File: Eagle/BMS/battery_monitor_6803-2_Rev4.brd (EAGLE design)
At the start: 69.5 x 53.3 mm, 66 parts, among them Q1 MOSFET-PCHANNELIRLML2244, Q10 IRF9530, Q2 MOSFET-NCHANNELBSS138, Q3 MOSFET-PCHANNELIRLML2244, Q4 MOSFET-PCHANNELIRLML2244, Q5 MOSFET-PCHANNELIRLML2244, Q6 MOSFET-NCHANNELBSS138, Q7 MOSFET-NCHANNELBSS138, Q8 MOSFET-NCHANNELBSS138, Q9 PMOS_AO4435

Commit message: Finished new BMS boards in Eagle.
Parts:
- moved R18 68.6 mm to (82.4, 51.4), turned to 90 degrees
- moved LED3 67.0 mm to (82.4, 48.6), turned to 180 degrees
- moved R17 65.7 mm to (80.1, 51.4), turned to 90 degrees
- moved LED2 64.0 mm to (80.1, 48.6), turned to 180 degrees
- moved R16 62.9 mm to (77.9, 51.4), turned to 90 degrees
- moved LED1 61.1 mm to (77.9, 48.6), turned to 180 degrees
- moved U$1 58.8 mm to (73.9, 34.8), turned to 0 degrees
- moved U$3 47.4 mm to (86.4, 34.8), turned to 0 degrees
- moved U$2 47.1 mm to (80.1, 34.8), turned to 180 degrees
- moved R24 1.73 mm to (30.7, 17.4)
- moved R23 1.53 mm to (33.0, 17.4)
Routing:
- net N$10: track 0.00 -> 83.7 mm, vias 0 -> 1
- net N$3: track 55.4 -> 133.8 mm, vias 2 -> 5
- net +5: track 71.0 -> 144.2 mm, vias 3 -> 4
- net N$12: track 0.00 -> 54.9 mm, vias 0 -> 2
- net GPIO2: track 0.00 -> 46.1 mm, vias 0 -> 3
- net N$2: track 36.2 -> 75.3 mm, vias 0 -> 2
- net N$5: track 0.00 -> 38.1 mm, vias 0 -> 1
- net GPIO1: track 0.00 -> 37.6 mm, vias 0 -> 4
- net A0: track 4.24 -> 41.8 mm, vias 1 -> 3
- net WDTB: track 0.00 -> 35.9 mm, vias 0 -> 4
- net N$29: track 0.00 -> 15.1 mm, vias 0 -> 2
- net S2: track 48.4 -> 36.9 mm, vias 3 -> 1
- net C12: track 41.9 -> 52.4 mm
- net SDA: track 57.0 -> 64.6 mm
- net VREF: track 29.7 -> 22.8 mm, vias 2 -> 3
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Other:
- board size 69.5 x 53.3 mm -> 89.8 x 53.3 mm
- board text added: "ITEST BMS Rev 4"
- board text removed: "ITEST BMS Rev 3"

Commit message: Final revisions on BMS boards.
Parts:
- moved U$1 0.28 mm to (74.0, 35.1)
- moved U$2 0.25 mm to (80.1, 35.1)
- moved U$3 0.25 mm to (86.4, 35.1)
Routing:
- net GND: track 137.4 -> 161.4 mm, vias 14 -> 13
- net N$3: track 133.8 -> 141.2 mm, vias 5 -> 6
- net N$12: track 54.9 -> 60.6 mm, vias 2 -> 1
- net CHARGER_IN: track 69.9 -> 64.9 mm
- net N$5: track 38.1 -> 35.6 mm
- net C1: track 87.5 -> 85.5 mm, vias 9 -> 6
- net ESTOP2: track 55.2 -> 53.5 mm, vias 4 -> 2
- net N$10: track 83.7 -> 82.4 mm
- net N$2: track 75.3 -> 74.4 mm, vias 2 -> 1
- net C2: track 87.7 -> 88.4 mm
- net S3: track 43.6 -> 43.1 mm
- net BATTERY+: track 16.2 -> 16.0 mm, vias 1 -> 0
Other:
- board size 89.8 x 53.3 mm -> 88.1 x 53.3 mm

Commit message: Latest BMS Rev3 and Rev4 edits.
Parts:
- R26: value 1MEG -> 1Meg
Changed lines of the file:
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@@
 <attribute name="PROD_ID" value="TRANS-11153" x="-74.168" y="-48.514" size="1.778" layer="27" rot="R270" display="off"/>
 <attribute name="NAME" x="47.625" y="41.9735" size="0.4064" layer="25" rot="R270"/>
-<attribute name="OC_NEWARK" value="40X8697" x="46.482" y="42.926" size="1.778" layer="27" rot="R270" display="off"/>
+<attribute name="OC_NEWARK" value="40T7448" x="46.482" y="42.926" size="1.778" layer="27" rot="R270" display="off"/>
 <attribute name="MF" value="" x="46.482" y="42.926" size="1.778" layer="27" rot="R270" display="off"/>
-<attribute name="MPN" value="SI2369DS-T1-GE3" x="46.482" y="42.926" size="1.778" layer="27" rot="R270" display="off"/>
+<attribute name="MPN" value="IRLML2244TRPBF" x="46.482" y="42.926" size="1.778" layer="27" rot="R270" display="off"/>
 </element>
 <element name="DZ1" library="SparkFun-DiscreteSemi" package="SOD-323" value="PDZ7.5B" x="34.798" y="46.482" smashed="yes" rot="R90">
@@
 <attribute name="PROD_ID" value="TRANS-11153" x="-87.63" y="21.209" size="1.778" layer="27" rot="R270" display="off"/>
 <attribute name="NAME" x="40.513" y="42.1005" size="0.4064" layer="25" rot="R270"/>
-<attribute name="OC_NEWARK" value="40X8697" x="39.37" y="42.799" size="1.778" layer="27" rot="R270" display="off"/>
+<attribute name="OC_NEWARK" value="40T7448" x="39.37" y="42.799" size="1.778" layer="27" rot="R270" display="off"/>
 <attribute name="MF" value="" x="39.37" y="42.799" size="1.778" layer="27" rot="R270" display="off"/>
-<attribute name="MPN" value="SI2369DS-T1-GE3" x="39.37" y="42.799" size="1.778" layer="27" rot="R270" display="off"/>
+<attribute name="MPN" value="IRLML2244TRPBF" x="39.37" y="42.799" size="1.778" layer="27" rot="R270" display="off"/>
 </element>
 <element name="Q5" library="SparkFun-DiscreteSemi" package="SOT23-3" value="MOSFET-PCHANNELIRLML2244" x="39.37" y="46.482" smashed="yes" rot="R270">
 <attribute name="PROD_ID" value="TRANS-11153" x="-87.63" y="14.732" size="1.778" layer="27" rot="R270" display="off"/>
 <attribute name="NAME" x="40.386" y="45.6565" size="0.4064" layer="25" rot="R270"/>
-<attribute name="OC_NEWARK" value="40X8697" x="39.37" y="46.482" size="1.778" layer="27" rot="R270" display="off"/>
+<attribute name="OC_NEWARK" value="40T7448" x="39.37" y="46.482" size="1.778" layer="27" rot="R270" display="off"/>
 <attribute name="MF" value="" x="39.37" y="46.482" size="1.778" layer="27" rot="R270" display="off"/>
-<attribute name="MPN" value="SI2369DS-T1-GE3" x="39.37" y="46.482" size="1.778" layer="27" rot="R270" display="off"/>
+<attribute name="MPN" value="IRLML2244TRPBF" x="39.37" y="46.482" size="1.778" layer="27" rot="R270" display="off"/>
 </element>
 <element name="R4" library="SparkFun-Resistors" package="0603-RES" value="100" x="22.352" y="38.862">
@@
 <attribute name="PROD_ID" value="TRANS-11153" x="109.093" y="-104.775" size="1.778" layer="27" display="off"/>
 <attribute name="NAME" x="28.5115" y="16.891" size="0.4064" layer="25"/>
-<attribute name="OC_NEWARK" value="40X8697" x="27.813" y="15.875" size="1.778" layer="27" display="off"/>
+<attribute name="OC_NEWARK" value="40T7448" x="27.813" y="15.875" size="1.778" layer="27" display="off"/>
 <attribute name="MF" value="" x="27.813" y="15.875" size="1.778" layer="27" display="off"/>
-<attribute name="MPN" value="SI2369DS-T1-GE3" x="27.813" y="15.875" size="1.778" layer="27" display="off"/>
+<attribute name="MPN" value="IRLML2244TRPBF" x="27.813" y="15.875" size="1.778" layer="27" display="off"/>
 </element>
 <element name="R8" library="SparkFun-Resistors" package="0603-RES" value="100" x="22.606" y="35.687" smashed="yes" rot="R180">
@@
 <attribute name="MPN" value="282834-2" x="5.08" y="19.558" size="1.778" layer="27" display="off"/>
 </element>
-<element name="R26" library="SparkFun-Resistors" package="0603-RES" value="1MEG" x="17.272" y="16.637" rot="R90">
+<element name="R26" library="SparkFun-Resistors" package="0603-RES" value="1Meg" x="17.272" y="16.637" rot="R90">
 <attribute name="PROD_ID" value="RES-07851" x="17.272" y="16.637" size="1.778" layer="27" rot="R90" display="off"/>
 <attribute name="OC_NEWARK" value="64R5311" x="17.272" y="16.637" size="1.778" layer="27" rot="R90" display="off"/>

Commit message: Latest BMS Rev3 and Rev4 edits.
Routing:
- net CHARGER_IN: track 64.9 -> 64.2 mm
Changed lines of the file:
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@@
 <wire x1="21.336" y1="15.494" x2="21.336" y2="12.192" width="0.6096" layer="1"/>
 <wire x1="21.336" y1="12.192" x2="21.082" y2="11.938" width="0.6096" layer="1"/>
-<wire x1="21.082" y1="11.938" x2="20.066" y2="11.938" width="0.6096" layer="1"/>
+<wire x1="21.082" y1="11.938" x2="20.828" y2="11.938" width="0.6096" layer="1"/>
+<wire x1="20.828" y1="11.938" x2="20.066" y2="11.938" width="0.6096" layer="1"/>
 <wire x1="22.606" y1="15.494" x2="22.606" y2="12.192" width="0.6096" layer="1"/>
 <wire x1="22.606" y1="12.192" x2="22.352" y2="11.938" width="0.6096" layer="1"/>
 <wire x1="22.352" y1="11.938" x2="21.59" y2="11.938" width="0.6096" layer="1"/>
-<wire x1="21.59" y1="11.938" x2="21.336" y2="12.192" width="0.6096" layer="1"/>
 <wire x1="13.716" y1="9.906" x2="14.732" y2="9.906" width="1.016" layer="1"/>
-<wire x1="14.732" y1="9.906" x2="20.955" y2="9.906" width="1.016" layer="1"/>
-<wire x1="20.955" y1="9.906" x2="21.082" y2="10.033" width="1.016" layer="1"/>
-<wire x1="21.082" y1="10.033" x2="21.082" y2="11.43" width="1.016" layer="1"/>
-<wire x1="21.082" y1="11.43" x2="21.59" y2="11.938" width="1.016" layer="1"/>
 <wire x1="23.071" y1="5.527" x2="19.111" y2="5.527" width="0.4064" layer="1"/>
 <wire x1="19.111" y1="5.527" x2="14.732" y2="9.906" width="0.4064" layer="1"/>
 <wire x1="13.716" y1="9.906" x2="10.033" y2="6.223" width="1.016" layer="1"/>
 <wire x1="10.033" y1="6.223" x2="4.953" y2="6.223" width="1.016" layer="1"/>
+<wire x1="14.732" y1="9.906" x2="19.558" y2="9.906" width="1.016" layer="1"/>
+<wire x1="19.558" y1="9.906" x2="21.59" y2="11.938" width="1.016" layer="1"/>
+<wire x1="21.59" y1="11.938" x2="21.082" y2="11.938" width="0.6096" layer="1"/>
 </signal>
 <signal name="GPIO2">

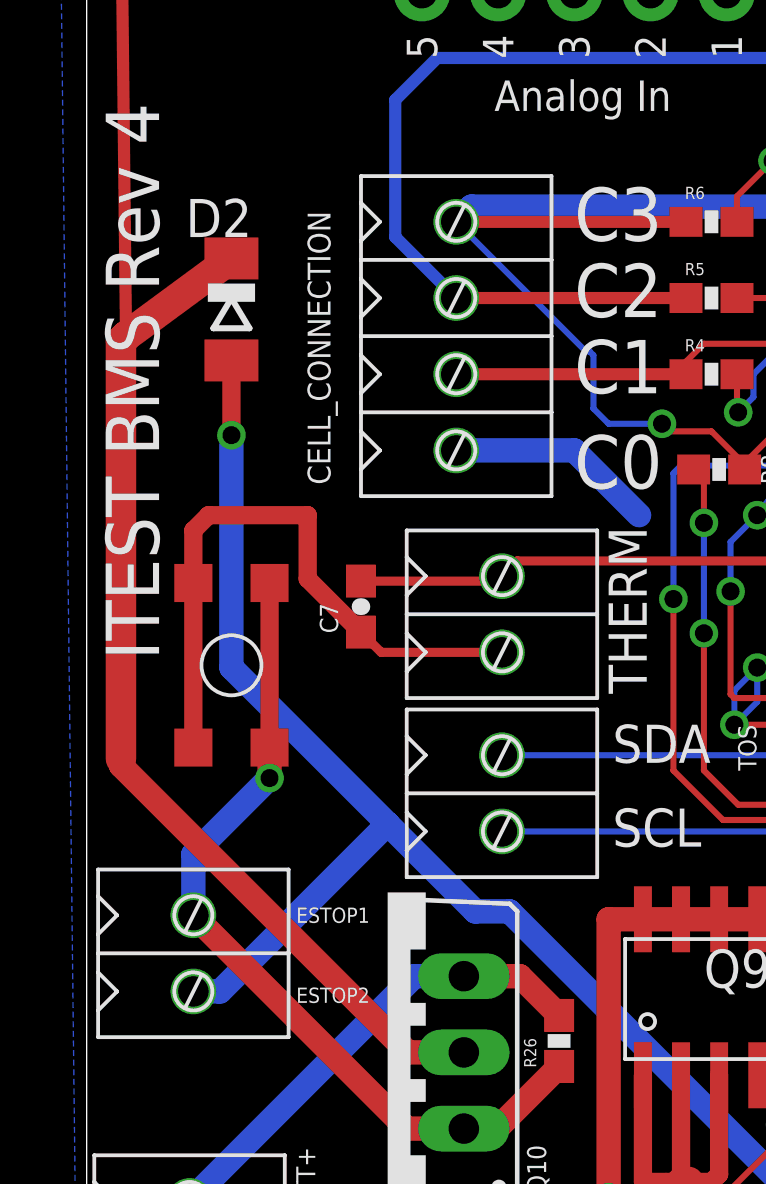
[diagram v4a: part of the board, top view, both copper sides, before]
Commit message: Fixed minor issues with BMS board and added magnetic encoder information.
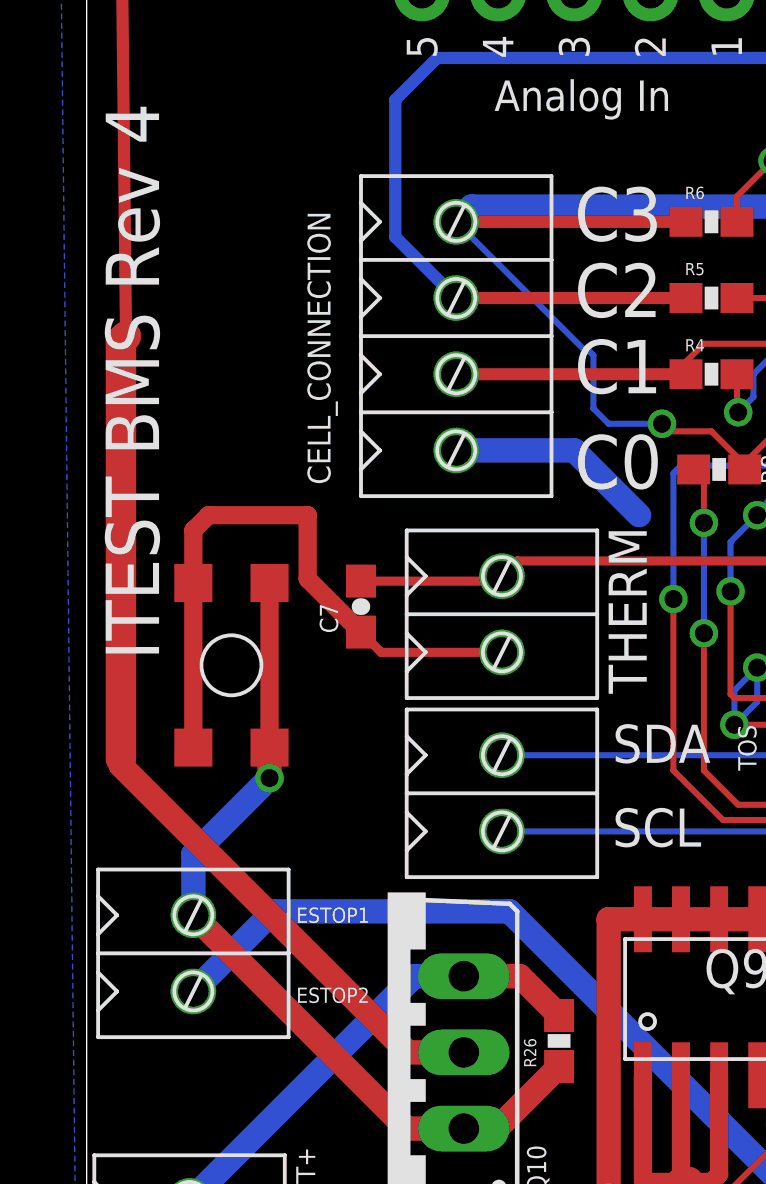
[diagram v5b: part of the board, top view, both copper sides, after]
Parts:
- removed D2: PMLL41SOD80C, diode:SOD80C
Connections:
- net +12: no longer D2.C
- net ESTOP2: no longer D2.A
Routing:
- net ESTOP2: track 53.5 -> 33.4 mm, vias 2 -> 1
- net +12: track 75.4 -> 71.0 mm
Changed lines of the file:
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@@
 <attribute name="MPN" value="CRCW06034K70FKEA" x="38.735" y="12.446" size="1.778" layer="27" rot="R180" display="off"/>
-</element>
-<element name="D2" library="diode" package="SOD80C" value="PMLL41SOD80C" x="6.35" y="41.021" smashed="yes" rot="R270">
-<attribute name="NAME" x="4.826" y="43.434" size="1.27" layer="25"/>
-<attribute name="OC_NEWARK" value="18C6408" x="6.35" y="41.021" size="1.778" layer="27" rot="R270" display="off"/>
-<attribute name="MF" value="FAIRCHILD SEMICONDUCTOR" x="6.35" y="41.021" size="1.778" layer="27" rot="R270" display="off"/>
-<attribute name="MPN" value="FDLL4148" x="6.35" y="41.021" size="1.778" layer="27" rot="R270" display="off"/>
 </element>
 <element name="I2C" library="isaac1" package="SCREW_TERMINAL_2" value="SCREW_TERMINAL_2" x="15.367" y="24.892" smashed="yes">
@@
 <signal name="+12">
 <contactref element="U$8" pad="VIN"/>
-<contactref element="D2" pad="C"/>
 <wire x1="30.48" y1="51.562" x2="30.48" y2="51.943" width="0.4064" layer="1"/>
 <wire x1="30.48" y1="51.943" x2="29.21" y2="53.213" width="0.4064" layer="1"/>
@@
 <wire x1="2.667" y1="26.035" x2="2.667" y2="39.96441875" width="1.016" layer="1"/>
 <wire x1="2.667" y1="39.96441875" x2="2.8357" y2="40.13311875" width="1.016" layer="1"/>
-<wire x1="2.8357" y1="40.13311875" x2="6.35" y2="42.721" width="1.016" layer="1"/>
 <wire x1="12.230846875" y1="16.256" x2="2.667" y2="25.819846875" width="0.8128" layer="1"/>
 <wire x1="2.667" y1="25.819846875" x2="2.667" y2="26.035" width="0.8128" layer="1"/>
@@
 <via x="31.115" y="11.811" extent="1-16" drill="0.6"/>
 <contactref element="U$6" pad="P$2"/>
-<via x="6.35" y="36.83" extent="1-16" drill="0.6"/>
-<contactref element="D2" pad="A"/>
 <contactref element="Q6" pad="3"/>
-<wire x1="6.35" y1="36.83" x2="6.35" y2="39.321" width="0.6096" layer="1"/>
-<wire x1="6.35" y1="36.83" x2="6.35" y2="29.083" width="0.8128" layer="16"/>
-<wire x1="6.35" y1="29.083" x2="11.557" y2="23.876" width="0.8128" layer="16"/>
-<wire x1="5.08" y1="18.288" x2="5.969" y2="18.288" width="0.8128" layer="16"/>
-<wire x1="5.969" y1="18.288" x2="11.557" y2="23.876" width="0.8128" layer="16"/>
-<wire x1="11.557" y1="23.876" x2="14.478" y2="20.955" width="0.8128" layer="16"/>
-<wire x1="14.478" y1="20.955" x2="15.621" y2="20.955" width="0.8128" layer="16"/>
 <wire x1="15.621" y1="20.955" x2="24.765" y2="11.811" width="0.8128" layer="16"/>
 <wire x1="24.765" y1="11.811" x2="31.115" y2="11.811" width="0.8128" layer="16"/>
+<wire x1="15.621" y1="20.955" x2="7.747" y2="20.955" width="0.8128" layer="16"/>
+<wire x1="7.747" y1="20.955" x2="5.08" y2="18.288" width="0.8128" layer="16"/>
 <wire x1="33.02" y1="13.462" x2="33.19" y2="13.462" width="0" layer="19" extent="1-1"/>
 </signal>
